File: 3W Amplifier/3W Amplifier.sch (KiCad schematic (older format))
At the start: 24 parts, among them U1 PAM8008

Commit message: Remove 0 ohm resistors from schematic
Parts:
- removed R2, R4, R5, R6, R7, R8: 0Ω, NewFootPrint:Resistor, symbol Device:R
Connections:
- wire segments 96 -> 91
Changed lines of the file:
@@
-$EndComp
-$Comp
-L Device:R R4
-U 1 1 5B734A03
-P 5150 3800
-F 0 "R4" V 4943 3800 50  0000 C CNN
-F 1 "0Ω" V 5034 3800 50  0000 C CNN
-F 2 "NewFootPrint:Resistor" V 5080 3800 50  0001 C CNN
-F 3 "~" H 5150 3800 50  0001 C CNN
-	1    5150 3800
-	0    1    1    0
-$EndComp
-$Comp
-L Device:R R2
-U 1 1 5B734A5F
-P 7700 4150
-F 0 "R2" V 7493 4150 50  0000 C CNN
-F 1 "0Ω" V 7600 4150 50  0000 C CNN
-F 2 "NewFootPrint:Resistor" V 7630 4150 50  0001 C CNN
-F 3 "~" H 7700 4150 50  0001 C CNN
-	1    7700 4150
-	0    1    1    0
 $EndComp
 $Comp
@@
 	7200 4100 7200 4150
 Wire Wire Line
-	7200 4150 7550 4150
-Wire Wire Line
 	7200 3900 7700 3900
 Wire Wire Line
@@
 Wire Wire Line
 	7350 5000 7500 5000
-Wire Wire Line
-	7200 3500 7450 3500
 Wire Wire Line
 	4000 3600 4000 4000
@@
 $EndComp
 Wire Wire Line
-	5000 3800 3850 3800
-Wire Wire Line
 	7500 4750 7500 5000
-Connection ~ 7750 3500
-Wire Wire Line
-	7750 3500 7750 2400
 Text Label 4700 2400 0    50   ~ 0
 VDD
@@
 	6200 4350 6200 3400
 Wire Wire Line
-	5300 3800 5350 3800
-Wire Wire Line
 	5350 3800 5350 4000
 Wire Wire Line
@@
 Wire Wire Line
 	6050 3600 6050 3450
-Wire Wire Line
-	6050 3450 5950 3450
 Wire Wire Line
 	4750 3450 4950 3450
@@
 	1    0    0    -1
 $EndComp
-Wire Wire Line
-	5950 3800 5950 4150
 Connection ~ 6200 5000
 Connection ~ 7250 5000
-$Comp
-L Device:R R5
-U 1 1 5BE8ED43
-P 5800 3450
-F 0 "R5" V 5593 3450 50  0000 C CNN
-F 1 "0Ω" V 5684 3450 50  0000 C CNN
-F 2 "NewFootPrint:Resistor" V 5730 3450 50  0001 C CNN
-F 3 "~" H 5800 3450 50  0001 C CNN
-	1    5800 3450
-	0    1    1    0
-$EndComp
-$Comp
-L Device:R R6
-U 1 1 5BE8EDDB
-P 5950 4300
-F 0 "R6" H 5880 4254 50  0000 R CNN
-F 1 "0Ω" H 5880 4345 50  0000 R CNN
-F 2 "NewFootPrint:Resistor" V 5880 4300 50  0001 C CNN
-F 3 "~" H 5950 4300 50  0001 C CNN
-	1    5950 4300
-	-1   0    0    1
-$EndComp
-Wire Wire Line
-	5650 3450 5250 3450
-Wire Wire Line
-	5950 4450 5950 5000
 Wire Wire Line
 	4750 5000 5650 5000
@@
 Connection ~ 8400 4150
 Wire Wire Line
-	7850 4150 8400 4150
-Wire Wire Line
 	6200 5000 7250 5000
-$Comp
-L Device:R R7
-U 1 1 5BF2155E
-P 3200 3350
-F 0 "R7" H 3130 3304 50  0000 R CNN
-F 1 "0Ω" H 3130 3395 50  0000 R CNN
-F 2 "NewFootPrint:Resistor" V 3130 3350 50  0001 C CNN
-F 3 "~" H 3200 3350 50  0001 C CNN
-	1    3200 3350
-	-1   0    0    1
-$EndComp
-Wire Wire Line
-	3200 3500 3200 3700
-$Comp
-L Device:R R8
-U 1 1 5BF27365
-P 7600 3500
-F 0 "R8" V 7500 3500 50  0000 R CNN
-F 1 "0Ω" V 7500 3650 50  0000 R CNN
-F 2 "NewFootPrint:Resistor" V 7530 3500 50  0001 C CNN
-F 3 "~" H 7600 3500 50  0001 C CNN
-	1    7600 3500
-	0    1    1    0
-$EndComp
-Wire Wire Line
-	7750 3500 7750 4000
 Wire Wire Line
 	7200 4000 7750 4000
@@
 GND
 Wire Wire Line
-	3200 2400 3200 3200
-Wire Wire Line
 	4000 2400 6200 2400
 Wire Wire Line
@@
 Wire Wire Line
 	6200 2400 7750 2400
+Wire Wire Line
+	7750 2400 7750 3500
+Wire Wire Line
+	3200 2400 3200 3700
+Wire Wire Line
+	3850 3800 5350 3800
+Wire Wire Line
+	5950 3800 5950 5000
+Wire Wire Line
+	5250 3450 6050 3450
+Wire Wire Line
+	7200 3500 7750 3500
+Connection ~ 7750 3500
+Wire Wire Line
+	7750 3500 7750 4000
+Wire Wire Line
+	7200 4150 8400 4150
 $EndSCHEMATC

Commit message: Correctly connect the audio jack
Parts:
- U1: symbol New_Library:PAM8008 -> 3W-Amplifier-rescue:PAM8008-New_Library
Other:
- moved on the sheet: A1, C1
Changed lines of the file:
@@
 $EndDescr
 $Comp
-L New_Library:PAM8008 U1
+L 3W-Amplifier-rescue:PAM8008-New_Library U1
 U 1 1 5B734811
 P 6800 3700
@@
 L Device:C C1
 U 1 1 5B734D22
-P 4900 4250
-F 0 "C1" V 4648 4250 50  0000 C CNN
-F 1 "100nf" V 4739 4250 50  0000 C CNN
-F 2 "NewFootPrint:Capacitor_1206" H 4938 4100 50  0001 C CNN
-F 3 "~" H 4900 4250 50  0001 C CNN
-	1    4900 4250
+P 5050 4150
+F 0 "C1" V 4798 4150 50  0000 C CNN
+F 1 "100nf" V 4889 4150 50  0000 C CNN
+F 2 "NewFootPrint:Capacitor_1206" H 5088 4000 50  0001 C CNN
+F 3 "~" H 5050 4150 50  0001 C CNN
+	1    5050 4150
 	0    1    1    0
 $EndComp
@@
 	6400 3900 5800 3900
 Wire Wire Line
-	5800 3900 5800 4250
-Wire Wire Line
-	5800 4250 5050 4250
-Wire Wire Line
 	3700 3650 3700 2400
 Wire Wire Line
@@
 	3200 2400 3700 2400
 Connection ~ 3700 2400
-Wire Wire Line
-	4700 4250 4750 4250
 $Comp
 L Device:R_POT R1
@@
 Text Label 3250 5000 0    50   ~ 0
 GND
-Text Label 5400 4250 0    50   ~ 0
+Text Label 5400 4150 0    50   ~ 0
 LINN
 Text Label 5350 3450 0    50   ~ 0
@@
 	5350 3800 5350 4000
 Wire Wire Line
-	4700 4150 4750 4150
-Wire Wire Line
-	4750 4150 4750 3450
-Wire Wire Line
 	6050 3600 6050 3450
 Wire Wire Line
 	4750 3450 4950 3450
-Wire Wire Line
-	4700 4350 4750 4350
 Wire Wire Line
 	4750 4350 4750 5000
@@
 F 3 "~" H 4500 4250 50  0001 C CNN
 	1    4500 4250
-	1    0    0    -1
+	1    0    0    1
 $EndComp
 Connection ~ 6200 5000
@@
 Wire Wire Line
 	7200 4150 8400 4150
+Wire Wire Line
+	4750 4350 4700 4350
+Wire Wire Line
+	4700 4250 4750 4250
+Wire Wire Line
+	4750 3450 4750 4250
+Wire Wire Line
+	4700 4150 4900 4150
+Wire Wire Line
+	5200 4150 5800 4150
+Wire Wire Line
+	5800 4150 5800 3900
 $EndSCHEMATC

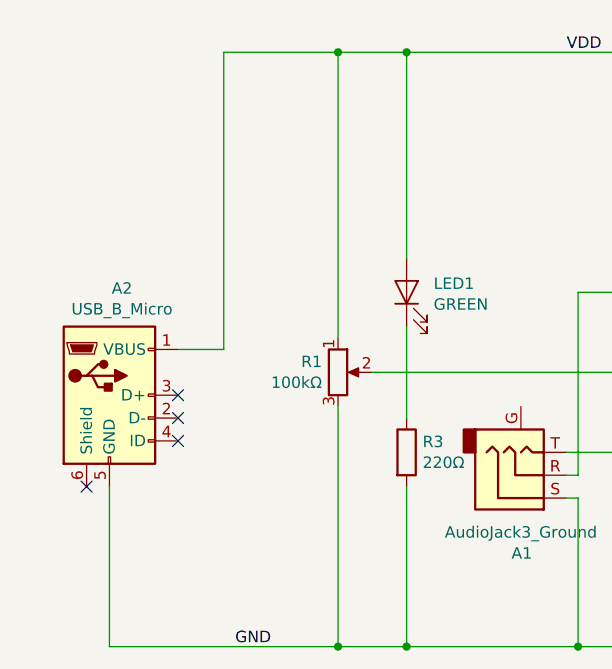
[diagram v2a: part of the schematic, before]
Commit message: add battery and switch to sch
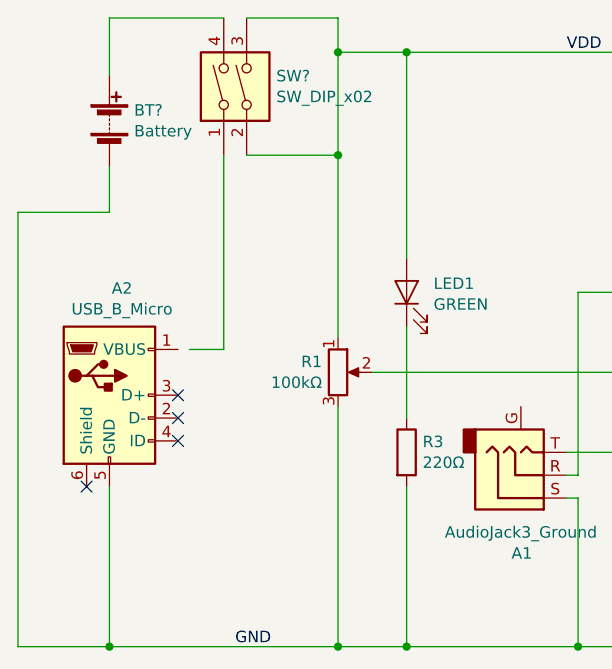
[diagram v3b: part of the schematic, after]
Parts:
- added BT?: Battery, symbol Device:Battery
- added SW?: SW_DIP_x02, symbol Switch:SW_DIP_x02
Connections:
- net GND: now also BT?.2 (-)
- net VDD: now also SW?.2, SW?.3; no longer A2.1 (VBUS)
- new net: BT?.1 (+), SW?.4
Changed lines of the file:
@@
 	6400 3900 5800 3900
 Wire Wire Line
-	3700 3650 3700 2400
+	3700 3650 3700 2850
 Wire Wire Line
 	3700 2400 4000 2400
@@
 	2700 4300 2700 5000
 Connection ~ 3700 5000
-Wire Wire Line
-	3000 3700 3200 3700
-Wire Wire Line
-	3200 2400 3700 2400
-Connection ~ 3700 2400
 $Comp
 L Device:R_POT R1
@@
 	7750 2400 7750 3500
 Wire Wire Line
-	3200 2400 3200 3700
-Wire Wire Line
 	3850 3800 5350 3800
 Wire Wire Line
@@
 Wire Wire Line
 	5800 4150 5800 3900
+$Comp
+L Switch:SW_DIP_x02 SW?
+U 1 1 5CB0BC2B
+P 3300 2550
+F 0 "SW?" V 3346 2420 50  0000 R CNN
+F 1 "SW_DIP_x02" V 3255 2420 50  0000 R CNN
+F 2 "" H 3300 2550 50  0001 C CNN
+F 3 "" H 3300 2550 50  0001 C CNN
+	1    3300 2550
+	0    -1   -1   0
+$EndComp
+$Comp
+L Device:Battery BT?
+U 1 1 5CB0BF96
+P 2700 2700
+F 0 "BT?" H 2808 2746 50  0000 L CNN
+F 1 "Battery" H 2808 2655 50  0000 L CNN
+F 2 "" V 2700 2760 50  0001 C CNN
+F 3 "~" V 2700 2760 50  0001 C CNN
+	1    2700 2700
+	1    0    0    -1
+$EndComp
+Wire Wire Line
+	2700 5000 2300 5000
+Wire Wire Line
+	2300 5000 2300 3100
+Wire Wire Line
+	2300 3100 2700 3100
+Wire Wire Line
+	2700 3100 2700 2900
+Connection ~ 2700 5000
+Wire Wire Line
+	3200 2250 2700 2250
+Wire Wire Line
+	2700 2250 2700 2500
+Wire Wire Line
+	3050 3700 3200 3700
+Wire Wire Line
+	3200 3700 3200 2850
+Wire Wire Line
+	3300 2850 3700 2850
+Connection ~ 3700 2850
+Wire Wire Line
+	3700 2850 3700 2400
+Wire Wire Line
+	3700 2400 3700 2250
+Wire Wire Line
+	3700 2250 3300 2250
+Connection ~ 3700 2400
 $EndSCHEMATC
